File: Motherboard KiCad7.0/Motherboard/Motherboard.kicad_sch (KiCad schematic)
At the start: 50 parts, among them J1 USB_B_Micro, J10 SWD_01x04_Pin, J2 B04B-XASK-1, J3 430450200, J4 430450200, Q8 AO4447A, SW1 SW_STM_BOOT_MODE, SW3 SW_STM_BOOT_MODE, U1 STM32F103CBT6, U2 AMS1117-3.3, U3 LM66100DCKR, U4 LM66100DCKR, U5 LM66100DCKR, Y1 X322516MMB4SI

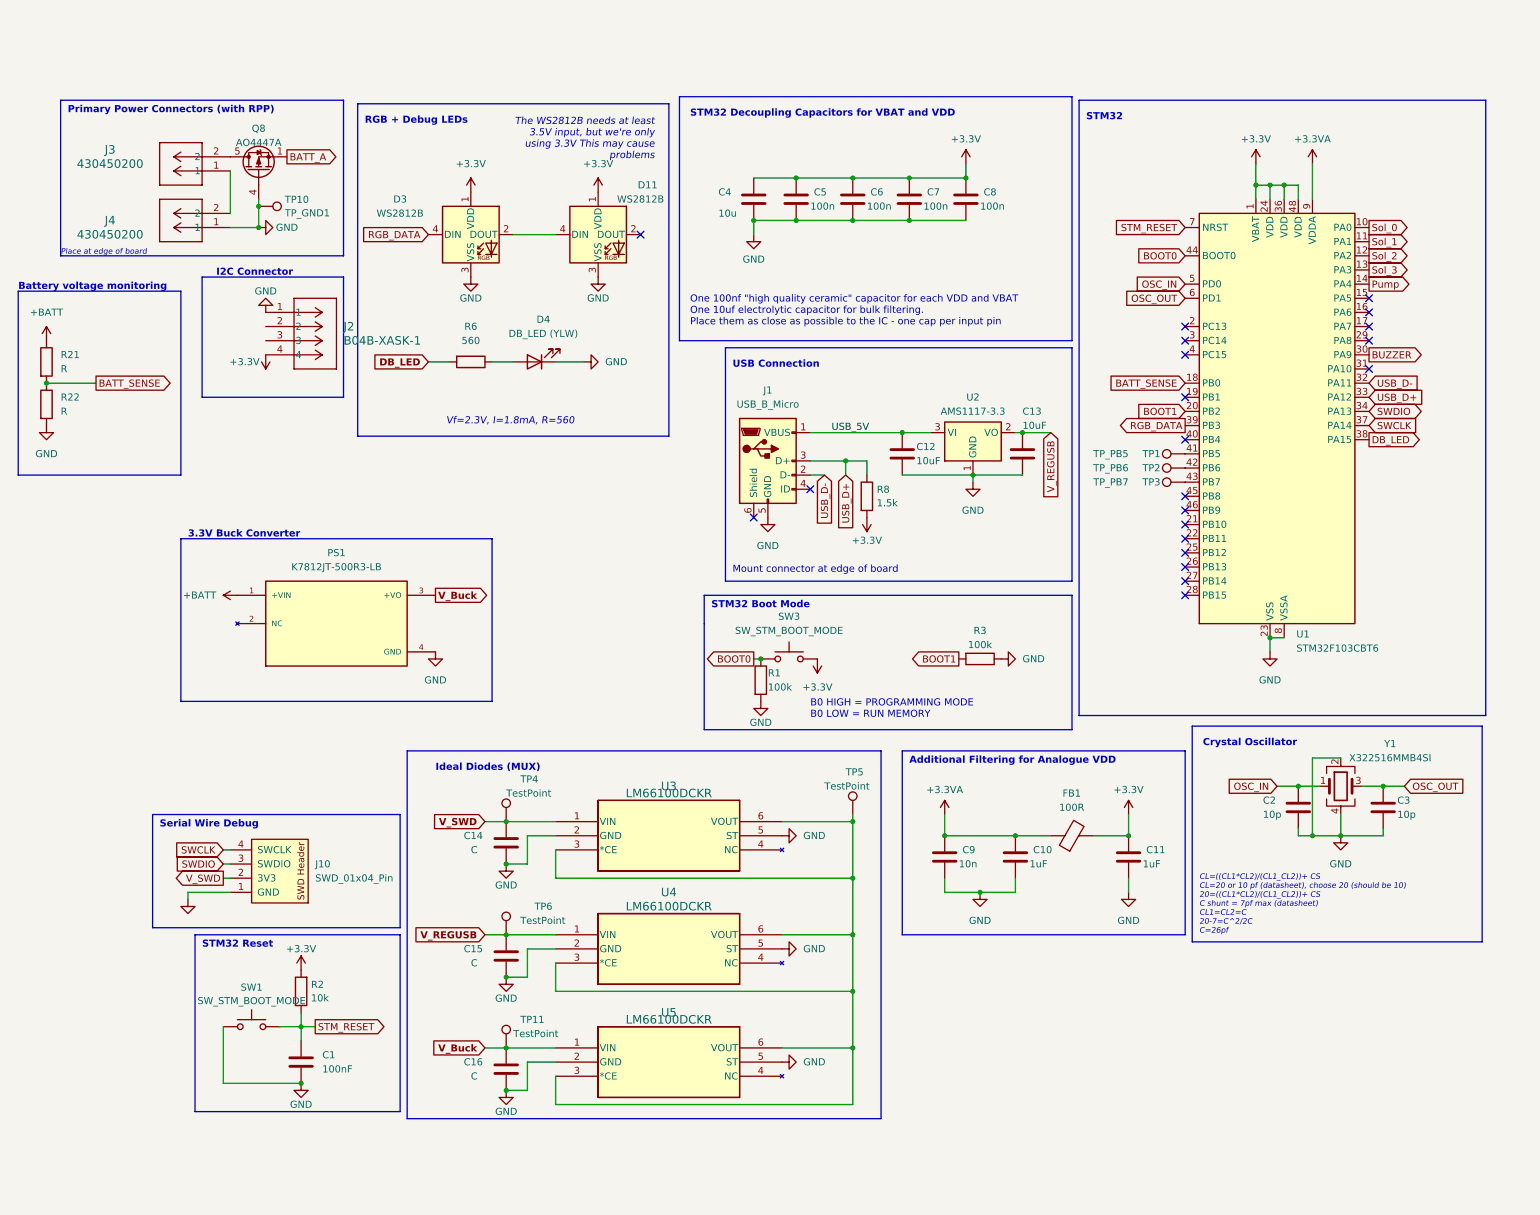
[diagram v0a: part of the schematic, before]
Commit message: Added MicroSD reader and part numbers
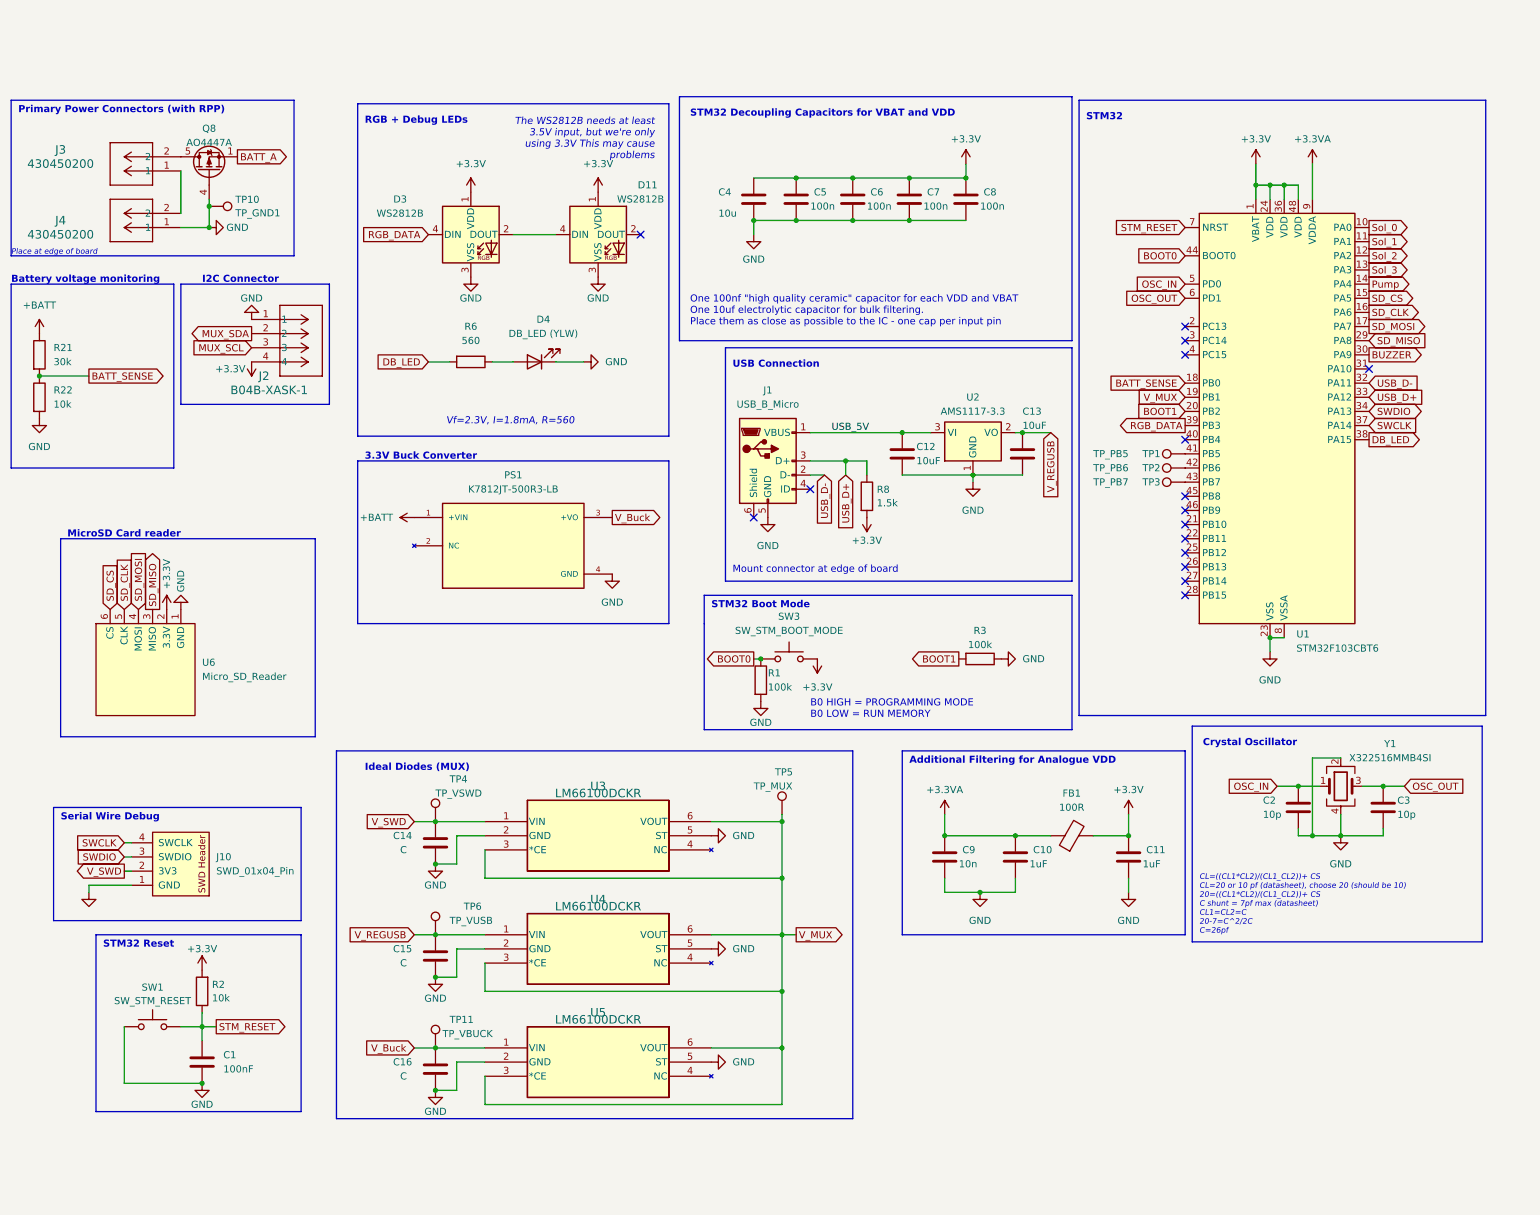
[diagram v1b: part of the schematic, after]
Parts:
- added U6: Micro_SD_Reader, MicroSD Card Reader:MicroSD Card Reader, symbol MicroSD Card Reader:Micro_SD_Reader
- C10, C11: footprint Capacitor_SMD:CP_Elec_4x5.4 -> Capacitor_SMD:C_0805_2012Metric
- C14, C15, C16: footprint (none) -> Capacitor_SMD:C_0603_1608Metric; LCSC (none) -> C15849
- D4: footprint (none) -> LED_SMD:LED_0603_1608Metric; LCSC (none) -> C72038
- J10: Digikey (none) -> 2057-PH1RB-04-UA-ND
- PS1: footprint K7812JT-500R3-LB:CONV_K7812JT-500R3-LB -> CONV_K7812JT-500R3-LB:CONV_K7812JT-500R3-LB; LCSC (none) -> C5127634
- R1, R3: footprint (none) -> Resistor_SMD:R_0603_1608Metric; LCSC (none) -> C25803
- R21: value R -> 30k
- R22: value R -> 10k
- R6: footprint (none) -> Resistor_SMD:R_0603_1608Metric; LCSC (none) -> C23204
- SW1: value SW_STM_BOOT_MODE -> SW_STM_RESET
- TP11: value TestPoint -> TP_VBUCK; footprint (none) -> TestPoint:TestPoint_Pad_1.5x1.5mm
- TP4: value TestPoint -> TP_VSWD; footprint (none) -> TestPoint:TestPoint_Pad_1.5x1.5mm
- TP5: value TestPoint -> TP_MUX; footprint (none) -> TestPoint:TestPoint_Pad_1.5x1.5mm
- TP6: value TestPoint -> TP_VUSB; footprint (none) -> TestPoint:TestPoint_Pad_1.5x1.5mm
- U3, U4, U5: Digikey (none) -> 296-53541-1-ND
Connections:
- net +3.3V: now also U6.2 (3.3V)
- net GND: now also U6.1 (GND)
- net V_MUX: now reaches TP5.1, U3.3 (*CE), U3.6 (VOUT), U4.3 (*CE), U4.6 (VOUT), U5.3 (*CE), U5.6 (VOUT)
- net V_MUX: now also U1.19 (PB1)
- net MUX_SDA: now reaches J2.2
- net MUX_SCL: now reaches J2.3
- net SD_CS: now reaches U1.15 (PA5)
- net SD_CS: now also U6.6 (CS)
- net SD_CLK: now reaches U1.16 (PA6)
- net SD_CLK: now also U6.5 (CLK)
- net SD_MOSI: now reaches U1.17 (PA7)
- net SD_MOSI: now also U6.4 (MOSI)
- net SD_MISO: now reaches U1.29 (PA8)
- net SD_MISO: now also U6.3 (MISO)
- no-connect marks 21 -> 16
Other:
- note added: "MicroSD Card reader"
- moved on the sheet: C1, C14, C15, C16, J10, J2, J3, J4, PS1, Q8, R2, R21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

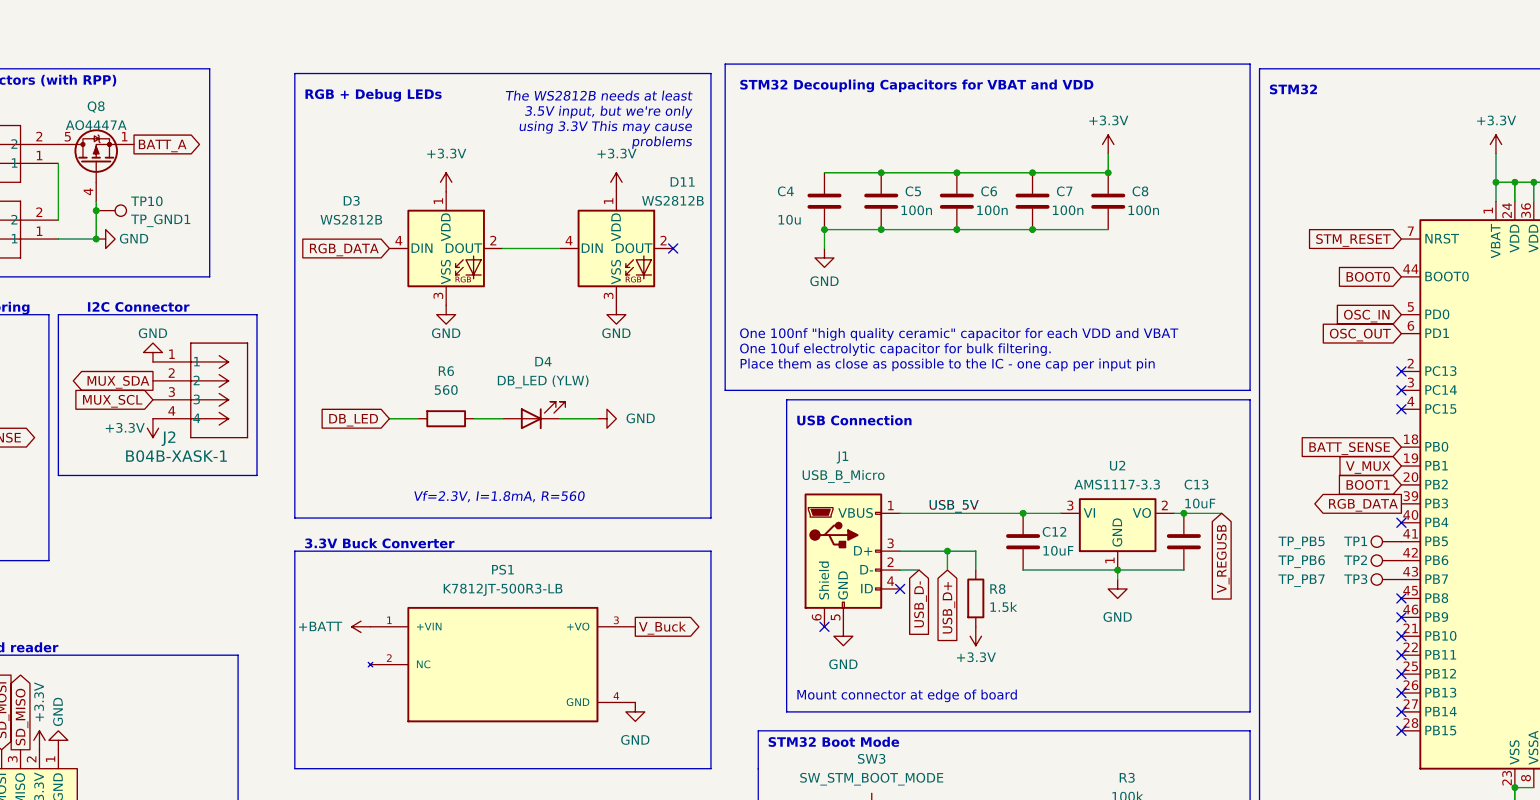
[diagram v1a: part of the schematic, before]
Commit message: Updated net labels
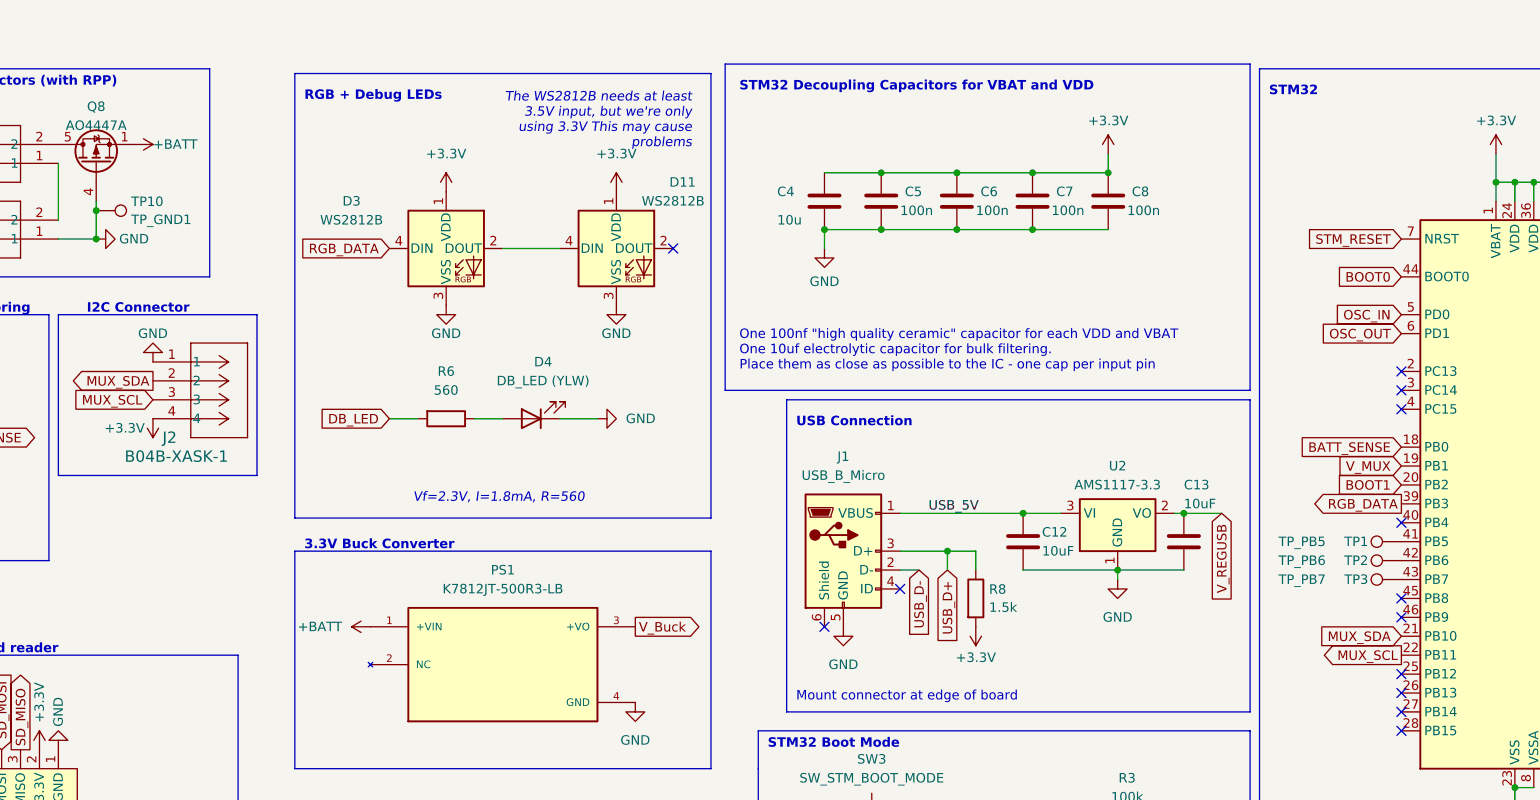
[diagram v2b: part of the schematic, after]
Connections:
- net BATT_A is gone; now on net +BATT: Q8.1 (S), Q8.2 (S), Q8.3 (S)
- net MUX_SCL: now also U1.22 (PB11)
- net MUX_SDA: now also U1.21 (PB10)
- no-connect marks 16 -> 14
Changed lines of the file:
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@@
   (no_connect (at 229.87 59.69))
   (no_connect (at 229.87 85.09))
-  (no_connect (at 229.87 92.71))
   (no_connect (at 229.87 74.93))
   (no_connect (at 229.87 102.87))
@@
   (no_connect (at 229.87 97.79))
   (no_connect (at 152.4 88.9))
-  (no_connect (at 229.87 90.17))
   (no_connect (at 229.87 57.15))
   (wire (pts (xy 265.43 146.05) (xy 257.81 146.05))
@@
     )
   )
+  (global_label "MUX_SDA" (shape input) (at 229.87 90.17 180) (fields_autoplaced)
+    (effects (font (size 1.27 1.27)) (justify right))
+    (property "Intersheetrefs" "${INTERSHEET_REFS}" (at 218.3577 90.17 0)
+      (effects (font (size 1.27 1.27)) (justify right) hide)
+    )
+  )
   (global_label "SD_CLK" (shape output) (at 262.89 52.07 0) (fields_autoplaced)
     (effects (font (size 1.27 1.27)) (justify left))
@@
     )
   )
-  (global_label "BATT_A" (shape output) (at 59.69 24.13 0) (fields_autoplaced)
-    (effects (font (size 1.27 1.27)) (justify left))
-    (property "Intersheetrefs" "${INTERSHEET_REFS}" (at 69.0252 24.13 0)
-      (effects (font (size 1.27 1.27)) (justify left) hide)
-    )
-  )
   (global_label "BATT_SENSE" (shape input) (at 229.87 64.77 180) (fields_autoplaced)
     (effects (font (size 1.27 1.27)) (justify right))
@@
     (effects (font (size 1.27 1.27)) (justify right))
     (property "Intersheetrefs" "${INTERSHEET_REFS}" (at 81.8629 184.15 0)
+      (effects (font (size 1.27 1.27)) (justify right) hide)
+    )
+  )
+  (global_label "MUX_SCL" (shape output) (at 229.87 92.71 180) (fields_autoplaced)
+    (effects (font (size 1.27 1.27)) (justify right))
+    (property "Intersheetrefs" "${INTERSHEET_REFS}" (at 218.4182 92.71 0)
       (effects (font (size 1.27 1.27)) (justify right) hide)
     )
@@
         )
       )
+    )
+  )
+  (symbol (lib_id "power:+BATT") (at 59.69 24.13 270) (unit 1)
+    (in_bom yes) (on_board yes) (dnp no)
+    (property "Reference" "#PWR051" (at 55.88 24.13 0)
+      (effects (font (size 1.27 1.27)) hide)
+    )
+    (property "Value" "+BATT" (at 62.23 24.13 90)
+      (effects (font (size 1.27 1.27)) (justify left))
+    )
+    (property "Footprint" "" (at 59.69 24.13 0)
+      (effects (font (size 1.27 1.27)) hide)
+    )
+    (property "Datasheet" "" (at 59.69 24.13 0)
+      (effects (font (size 1.27 1.27)) hide)
+    )
+    (pin "1")
+    (instances
+      (project "Motherboard"
+        (path "/6c6aab7b-9fc7-4161-8073-41667e18c629"
+          (reference "#PWR051") (unit 1)
+        )
+      )

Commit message: Corrected some silly mistakes
Fixed part numbers, some net label issues, resistor/capacitor values, type of buck converter used (was accidentally using 12V instead of 3.3V lol) and pinout of STM32.
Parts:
- added BZ1: PKM13EPYH4000, Buzzer_12.6x9.5RM5.0:Buzzer_12.6x9.5RM5.0, symbol Device:Buzzer
- added D10, D12, D13, D14, D15, D16, D17: 1N5819WS, Diode_SMD:D_SOD-323, symbol Diode:1N5819WS
- added J11, J12, J13, J14, J15: 430450200, CON_430450200_MOL, symbol CONN 0430450200:430450200
- added Q10, Q11, Q12, Q13, Q7, Q9: AO3400A, Package_TO_SOT_SMD:SOT-23, symbol Transistor_FET:AO3400A
- added R19, R23, R24, R25, R26, R27: 10k, Resistor_SMD:R_0603_1608Metric, symbol Device:R
- added R20, R28, R29, R30, R31, R32: 510R, Resistor_SMD:R_0603_1608Metric, symbol Device:R
- added R33: 1k, Resistor_SMD:R_0603_1608Metric, symbol Device:R
- C14, C15, C16: value C -> 1uF
- J2: footprint CONN_B04B-XASK-1_JST -> B04B_XASK_1:CONN_B04B-XASK-1_JST; LCSC (none) -> C264994
- J3: footprint CON_430450200_MOL -> CONN 0430450200:CON_430450200_MOL; LCSC (none) -> C122431
- J4: LCSC (none) -> C122431
- PS1: value K7812JT-500R3-LB -> K7803JT-500R3-LB; Digikey (none) -> 2725-K7803JT-500R3-LBCT-ND; LCSC C5127634 -> (none)
- R21: LCSC (none) -> C22984
- R22: LCSC (none) -> C25804
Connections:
- net +3.3V: now also TP5.1, U3.3 (*CE), U3.6 (VOUT), U4.3 (*CE), U4.6 (VOUT), U5.3 (*CE), U5.6 (VOUT), D12.2 (A)
- net +BATT: now also D10.2 (A), D13.1 (K), D14.1 (K), D15.1 (K), D16.1 (K), D17.1 (K), J11.1, J12.1, J13.1, J14.1, J15.1
- net BUZZER: now also R19.2, R20.2
- net GND: now also Q10.2 (S), Q11.2 (S), Q12.2 (S), Q13.2 (S), Q7.2 (S), Q9.2 (S), R19.1, R23.1, R24.1, R25.1, R26.1, R27.1
- net MUX_SCL: now also U1.21 (PB10); no longer U1.22 (PB11)
- net MUX_SDA: now also U1.22 (PB11); no longer U1.21 (PB10)
- net Pump: now also U1.29 (PA8), R27.2, R32.2; no longer U1.14 (PA4)
- net SD_CLK: now also U1.15 (PA5); no longer U1.16 (PA6)
- net SD_CS: now also U1.14 (PA4); no longer U1.15 (PA5)
- net SD_MISO: now also U1.16 (PA6); no longer U1.29 (PA8)
- net Sol_0: now also R23.2, R28.2
- net Sol_1: now also R24.2, R29.2
- net Sol_2: now also R25.2, R30.2
- net Sol_3: now also R26.2, R31.2
- removed net V_MUX: TP5.1, U1.19 (PB1), U3.3 (*CE), U3.6 (VOUT), U4.3 (*CE), U4.6 (VOUT), U5.3 (*CE), U5.6 (VOUT)
- new net: Q7.1 (G), R20.1
- new net: Q10.1 (G), R29.1
- new net: D14.2 (A), J12.2, Q10.3 (D)
- new net: D13.2 (A), J11.2, Q9.3 (D)
- new net: Q11.1 (G), R30.1
- new net: D15.2 (A), J13.2, Q11.3 (D)
- new net: D17.2 (A), J15.2, Q13.3 (D)
- new net: Q13.1 (G), R32.1
- new net: Q12.1 (G), R31.1
- new net: D16.2 (A), J14.2, Q12.3 (D)
- new net: Q9.1 (G), R28.1
- new net: BZ1.1 (+), D10.1 (K), D12.1 (K), R33.2
- new net: BZ1.2 (-), Q7.3 (D), R33.1
- no-connect marks 14 -> 15
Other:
- removed sheet Motherboard P2
- note added: "Air Pump"
- note added: "Buzzer"
- note added: "Solenoid Valves"
- company: (none) -> Queen's Rocket Engineering Team
- moved on the sheet: C1, C10, C11, C12, C13, C14, C15, C16, C2, C3, C4, C5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
